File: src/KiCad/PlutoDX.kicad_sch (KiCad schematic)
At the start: 0 parts

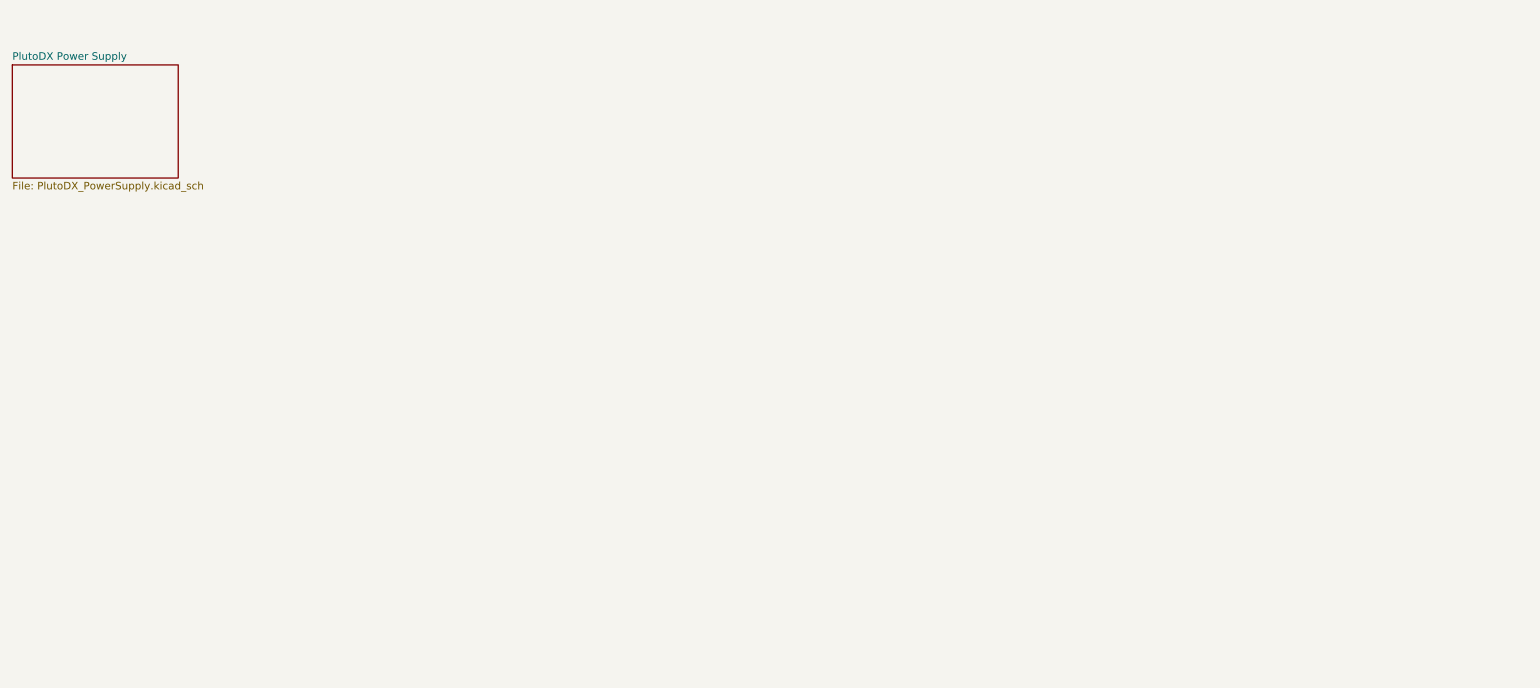
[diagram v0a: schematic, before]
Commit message: Import SOM304RD-VI symbol from the weeCee project
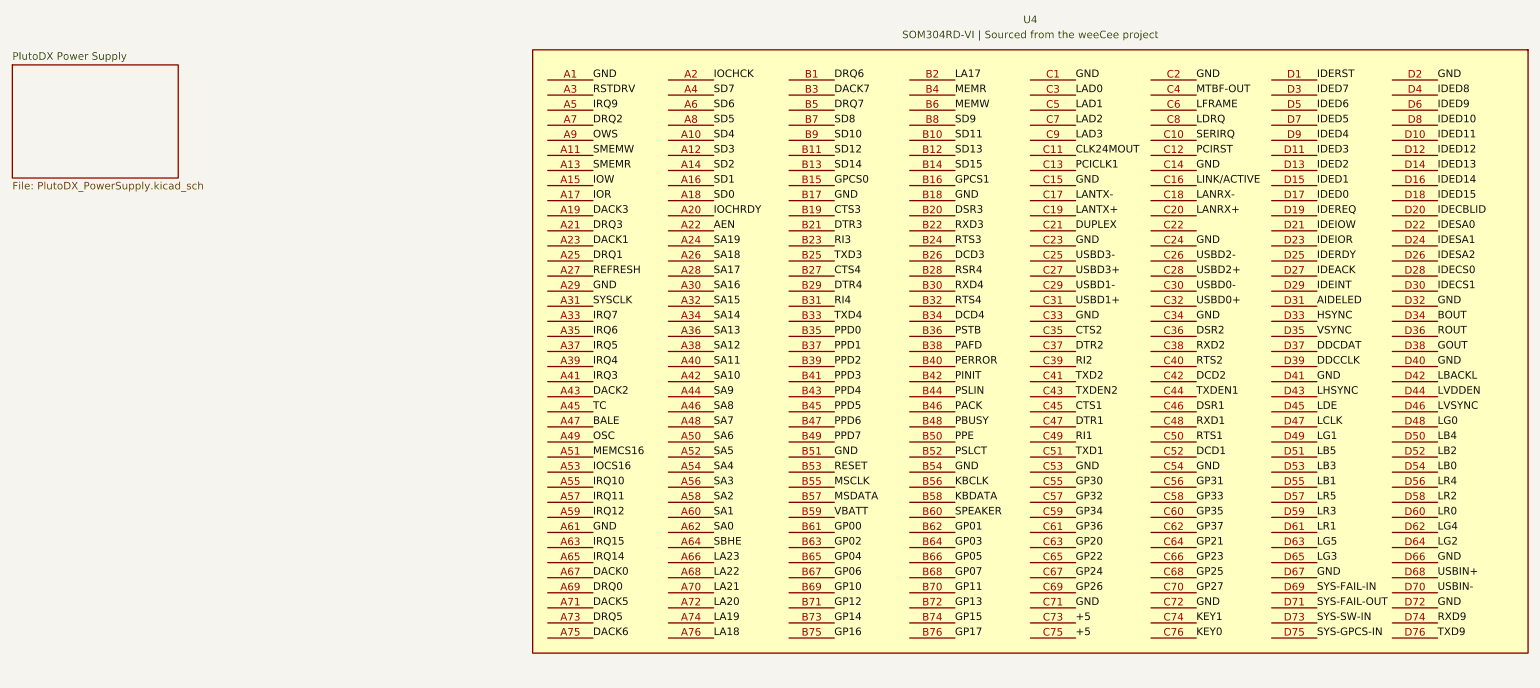
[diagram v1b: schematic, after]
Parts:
- added U4: SOM304RD-VI | Sourced from the weeCee project, Quad20, symbol SOM304RD-VI:SYM-7hfih1o77usjfiwb5d4g-1
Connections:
- new net +5: U4.C73, U4.C75
- new net AEN: U4.A22
- new net AIDELED: U4.D31
- new net BALE: U4.A47
- new net BOUT: U4.D34
- new net CLK24MOUT: U4.C11
- new net CTS1: U4.C45
- new net CTS2: U4.C35
- new net CTS3: U4.B19
- new net CTS4: U4.B27
- new net DACK0: U4.A67
- new net DACK1: U4.A23
- new net DACK2: U4.A43
- new net DACK3: U4.A19
- new net DACK5: U4.A71
- new net DACK6: U4.A75
- new net DACK7: U4.B3
- new net DCD1: U4.C52
- new net DCD2: U4.C42
- new net DCD3: U4.B26
- new net DCD4: U4.B34
- new net DDCCLK: U4.D39
- new net DDCDAT: U4.D37
- new net DRQ0: U4.A69
- new net DRQ1: U4.A25
- new net DRQ2: U4.A7
- new net DRQ3: U4.A21
- new net DRQ5: U4.A73
- new net DRQ6: U4.B1
- new net DRQ7: U4.B5
- new net DSR1: U4.C46
- new net DSR2: U4.C36
- new net DSR3: U4.B20
- new net DTR1: U4.C47
- new net DTR2: U4.C37
- new net DTR3: U4.B21
- new net DTR4: U4.B29
- new net DUPLEX: U4.C21
- new net GND: U4.A1, U4.A29, U4.A61, U4.B17, U4.B18, U4.B51, U4.B54, U4.C1, U4.C14, U4.C15, U4.C2, U4.C23, U4.C24, U4.C33, U4.C34, U4.C53, U4.C54, U4.C71, U4.C72, U4.D2, U4.D32, U4.D40, U4.D41, U4.D66, U4.D67, U4.D72
- new net GOUT: U4.D38
- new net GP00: U4.B61
- new net GP01: U4.B62
- new net GP02: U4.B63
- new net GP03: U4.B64
- new net GP04: U4.B65
- new net GP05: U4.B66
- new net GP06: U4.B67
- new net GP07: U4.B68
- new net GP10: U4.B69
- new net GP11: U4.B70
- new net GP12: U4.B71
- new net GP13: U4.B72
- new net GP14: U4.B73
- new net GP15: U4.B74
- new net GP16: U4.B75
- new net GP17: U4.B76
- new net GP20: U4.C63
- new net GP21: U4.C64
- new net GP22: U4.C65
- new net GP23: U4.C66
- new net GP24: U4.C67
- new net GP25: U4.C68
- new net GP26: U4.C69
- new net GP27: U4.C70
- new net GP30: U4.C55
- new net GP31: U4.C56
- new net GP32: U4.C57
- new net GP33: U4.C58
- new net GP34: U4.C59
- new net GP35: U4.C60
- new net GP36: U4.C61
- new net GP37: U4.C62
- new net GPCS0: U4.B15
- new net GPCS1: U4.B16
- new net HSYNC: U4.D33
- new net IDEACK: U4.D27
- new net IDECBLID: U4.D20
- new net IDECS0: U4.D28
- new net IDECS1: U4.D30
- new net IDED0: U4.D17
- new net IDED1: U4.D15
- new net IDED10: U4.D8
- new net IDED11: U4.D10
- new net IDED12: U4.D12
- new net IDED13: U4.D14
- new net IDED14: U4.D16
- new net IDED15: U4.D18
- new net IDED2: U4.D13
- new net IDED3: U4.D11
- new net IDED4: U4.D9
- new net IDED5: U4.D7
- new net IDED6: U4.D5
- new net IDED7: U4.D3
- new net IDED8: U4.D4
- new net IDED9: U4.D6
- new net IDEINT: U4.D29
- new net IDEIOR: U4.D23
- new net IDEIOW: U4.D21
- new net IDERDY: U4.D25
- new net IDEREQ: U4.D19
- new net IDERST: U4.D1
- new net IDESA0: U4.D22
- new net IDESA1: U4.D24
- new net IDESA2: U4.D26
- new net IOCHCK: U4.A2
- new net IOCHRDY: U4.A20
- new net IOCS16: U4.A53
- new net IOR: U4.A17
- new net IOW: U4.A15
- new net IRQ10: U4.A55
- new net IRQ11: U4.A57
- new net IRQ12: U4.A59
- new net IRQ14: U4.A65
- new net IRQ15: U4.A63
- new net IRQ3: U4.A41
- new net IRQ4: U4.A39
- new net IRQ5: U4.A37
- new net IRQ6: U4.A35
- new net IRQ7: U4.A33
- new net IRQ9: U4.A5
- new net KBCLK: U4.B56
- new net KBDATA: U4.B58
- new net KEY0: U4.C76
- new net KEY1: U4.C74
- new net LA17: U4.B2
- new net LA18: U4.A76
- new net LA19: U4.A74
- new net LA20: U4.A72
- new net LA21: U4.A70
- new net LA22: U4.A68
- new net LA23: U4.A66
- new net LAD0: U4.C3
- new net LAD1: U4.C5
- new net LAD2: U4.C7
- new net LAD3: U4.C9
- new net LANRX+: U4.C20
- new net LANRX-: U4.C18
- new net LANTX+: U4.C19
- new net LANTX-: U4.C17
- new net LB0: U4.D54
- new net LB1: U4.D55
- new net LB2: U4.D52
- new net LB3: U4.D53
- new net LB4: U4.D50
- new net LB5: U4.D51
- new net LBACKL: U4.D42
- new net LCLK: U4.D47
- new net LDE: U4.D45
- new net LDRQ: U4.C8
- new net LFRAME: U4.C6
- new net LG0: U4.D48
- new net LG1: U4.D49
- new net LG2: U4.D64
- new net LG3: U4.D65
- new net LG4: U4.D62
- new net LG5: U4.D63
- new net LHSYNC: U4.D43
- new net LINK/ACTIVE: U4.C16
- new net LR0: U4.D60
- new net LR1: U4.D61
- new net LR2: U4.D58
- new net LR3: U4.D59
- new net LR4: U4.D56
- new net LR5: U4.D57
- new net LVDDEN: U4.D44
- new net LVSYNC: U4.D46
- new net MEMCS16: U4.A51
- new net MEMR: U4.B4
- new net MEMW: U4.B6
- new net MSCLK: U4.B55
- new net MSDATA: U4.B57
- new net MTBF-OUT: U4.C4
- new net OSC: U4.A49
- new net OWS: U4.A9
- new net PACK: U4.B46
- new net PAFD: U4.B38
- new net PBUSY: U4.B48
- new net PCICLK1: U4.C13
- new net PCIRST: U4.C12
- new net PERROR: U4.B40
- new net PINIT: U4.B42
- new net PPD0: U4.B35
- new net PPD1: U4.B37
- new net PPD2: U4.B39
- new net PPD3: U4.B41
- new net PPD4: U4.B43
- new net PPD5: U4.B45
- new net PPD6: U4.B47
- new net PPD7: U4.B49
- new net PPE: U4.B50
- new net PSLCT: U4.B52
- new net PSLIN: U4.B44
- new net PSTB: U4.B36
- new net REFRESH: U4.A27
- new net RESET: U4.B53
- new net RI1: U4.C49
- new net RI2: U4.C39
- new net RI3: U4.B23
- new net RI4: U4.B31
- new net ROUT: U4.D36
- new net RSR4: U4.B28
- new net RSTDRV: U4.A3
- new net RTS1: U4.C50
- new net RTS2: U4.C40
- new net RTS3: U4.B24
- new net RTS4: U4.B32
- new net RXD1: U4.C48
- new net RXD2: U4.C38
- new net RXD3: U4.B22
- new net RXD4: U4.B30
- new net RXD9: U4.D74
- new net SA0: U4.A62
- new net SA1: U4.A60
- new net SA10: U4.A42
- new net SA11: U4.A40
- new net SA12: U4.A38
- new net SA13: U4.A36
- new net SA14: U4.A34
- new net SA15: U4.A32
- new net SA16: U4.A30
- new net SA17: U4.A28
- new net SA18: U4.A26
- new net SA19: U4.A24
- new net SA2: U4.A58
- new net SA3: U4.A56
- new net SA4: U4.A54
- new net SA5: U4.A52
- new net SA6: U4.A50
- new net SA7: U4.A48
- new net SA8: U4.A46
- new net SA9: U4.A44
- new net SBHE: U4.A64
- new net SD0: U4.A18
- new net SD1: U4.A16
- new net SD10: U4.B9
- new net SD11: U4.B10
- new net SD12: U4.B11
- new net SD13: U4.B12
- new net SD14: U4.B13
- new net SD15: U4.B14
- new net SD2: U4.A14
- new net SD3: U4.A12
- new net SD4: U4.A10
- new net SD5: U4.A8
- new net SD6: U4.A6
- new net SD7: U4.A4
- new net SD8: U4.B7
- new net SD9: U4.B8
- new net SERIRQ: U4.C10
- new net SMEMR: U4.A13
- new net SMEMW: U4.A11
- new net SPEAKER: U4.B60
- new net SYS-FAIL-IN: U4.D69
- new net SYS-FAIL-OUT: U4.D71
- new net SYS-GPCS-IN: U4.D75
- new net SYS-SW-IN: U4.D73
- new net SYSCLK: U4.A31
- new net TC: U4.A45
- new net TXD1: U4.C51
- new net TXD2: U4.C41
- new net TXD3: U4.B25
- new net TXD4: U4.B33
- new net TXD9: U4.D76
- new net TXDEN1: U4.C44
- new net TXDEN2: U4.C43
- new net USBD0+: U4.C32
- new net USBD0-: U4.C30
- new net USBD1+: U4.C31
- new net USBD1-: U4.C29
- new net USBD2+: U4.C28
- new net USBD2-: U4.C26
- new net USBD3+: U4.C27
- new net USBD3-: U4.C25
- new net USBIN+: U4.D68
- new net USBIN-: U4.D70
- new net VBATT: U4.B59
- new net VSYNC: U4.D35

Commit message: Start SD-IDE interface
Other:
- added sheet PlutoDX SD to IDE Interface (PlutoDX_SD2IDE-Interface.kicad_sch)
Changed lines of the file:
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@@
+		)
+	)
+	(sheet
+		(at 24.13 54.61)
+		(size 27.94 19.05)
+		(exclude_from_sim no)
+		(in_bom yes)
+		(on_board yes)
+		(dnp no)
+		(fields_autoplaced yes)
+		(stroke
+			(width 0.1524)
+			(type solid)
+		)
+		(fill
+			(color 0 0 0 0)
+		)
+		(property "Sheetname" "PlutoDX SD to IDE Interface"
+			(at 24.13 53.8984 0)
+			(show_name no)
+			(do_not_autoplace no)
+			(effects
+				(font
+					(size 1.27 1.27)
+				)
+				(justify left bottom)
+			)
+		)
+		(property "Sheetfile" "PlutoDX_SD2IDE-Interface.kicad_sch"
+			(at 24.13 74.2446 0)
+			(show_name no)
+			(do_not_autoplace no)
+			(effects
+				(font
+					(size 1.27 1.27)
+				)
+				(justify left top)
+			)
+		)
+		(property "Field2" ""
+			(at 24.13 54.61 0)
+			(hide yes)
+			(show_name no)
+			(do_not_autoplace no)
+			(effects
+				(font
+					(size 1.27 1.27)
+				)
+			)
+		)
+		(property "Field3" ""
+			(at 24.13 54.61 0)
+			(hide yes)
+			(show_name no)
+			(do_not_autoplace no)
+			(effects
+				(font
+					(size 1.27 1.27)
+				)
+			)
+		)
+		(instances
+			(project "PlutoDX"
+				(path "/68463962-111b-48d5-8810-5302d4be8c60"
+					(page "3")
+				)
+			)
 		)
 	)

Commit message: Start serial & parallel
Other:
- added sheet PlutoDX Serial & Parallel IO (PlutoDX_IO-Serial-Parallel.kicad_sch)
- added sheet PlutoDX Video (PlutoDX_Video.kicad_sch)
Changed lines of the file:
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@@
+	)
+	(sheet
+		(at 24.13 81.28)
+		(size 27.94 19.05)
+		(exclude_from_sim no)
+		(in_bom yes)
+		(on_board yes)
+		(dnp no)
+		(fields_autoplaced yes)
+		(stroke
+			(width 0.1524)
+			(type solid)
+		)
+		(fill
+			(color 0 0 0 0)
+		)
+		(property "Sheetname" "PlutoDX Video"
+			(at 24.13 80.5684 0)
+			(show_name no)
+			(do_not_autoplace no)
+			(effects
+				(font
+					(size 1.27 1.27)
+				)
+				(justify left bottom)
+			)
+		)
+		(property "Sheetfile" "PlutoDX_Video.kicad_sch"
+			(at 24.13 100.9146 0)
+			(show_name no)
+			(do_not_autoplace no)
+			(effects
+				(font
+					(size 1.27 1.27)
+				)
+				(justify left top)
+			)
+		)
+		(instances
+			(project "PlutoDX"
+				(path "/68463962-111b-48d5-8810-5302d4be8c60"
+					(page "4")
+				)
+			)
+		)
 	)
 	(sheet
@@
 				)
 			)
+		)
+	)
+	(sheet
+		(at 24.13 106.68)
+		(size 27.94 20.32)
+		(exclude_from_sim no)
+		(in_bom yes)
+		(on_board yes)
+		(dnp no)
+		(fields_autoplaced yes)
+		(stroke
+			(width 0.1524)
+			(type solid)
+		)
+		(fill
+			(color 0 0 0 0)
+		)
+		(property "Sheetname" "PlutoDX Serial & Parallel IO"
+			(at 24.13 105.9684 0)
+			(show_name no)
+			(do_not_autoplace no)
+			(effects
+				(font
+					(size 1.27 1.27)
+				)
+				(justify left bottom)
+			)
+		)
+		(property "Sheetfile" "PlutoDX_IO-Serial-Parallel.kicad_sch"
+			(at 24.13 127.5846 0)
+			(show_name no)
+			(do_not_autoplace no)
+			(effects
+				(font
+					(size 1.27 1.27)
+				)
+				(justify left top)
+			)
+		)
+		(instances
+			(project "PlutoDX"
+				(path "/68463962-111b-48d5-8810-5302d4be8c60"
+					(page "5")
+				)
+			)

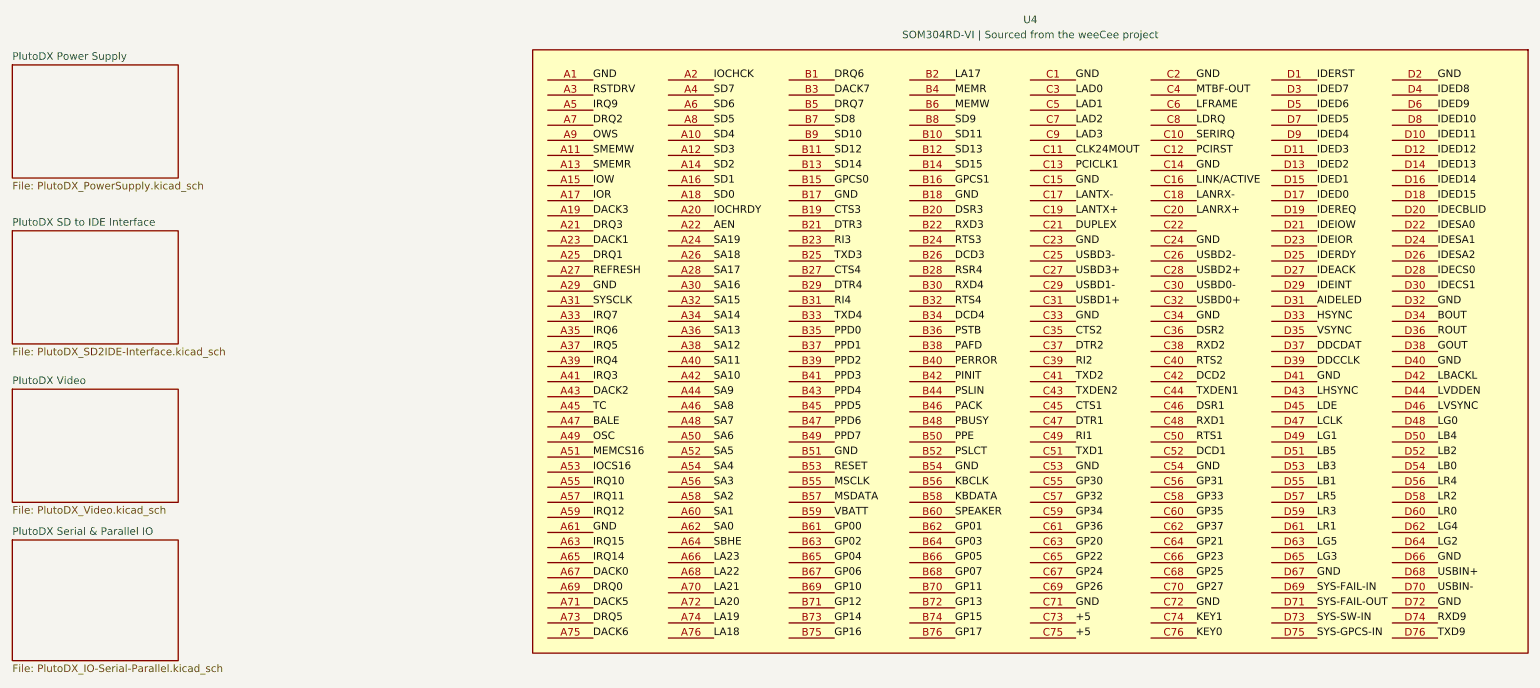
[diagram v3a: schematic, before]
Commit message: Switch to SOM304RD-PI fro mSOM304RD-VI
The SOM304RD-PI exposes a PCI bus, so PCI cards can be added. Video will now be handled via a PCI video card and/or 3D accelerator vs the SOM304RD-VI's built-in VGA video output
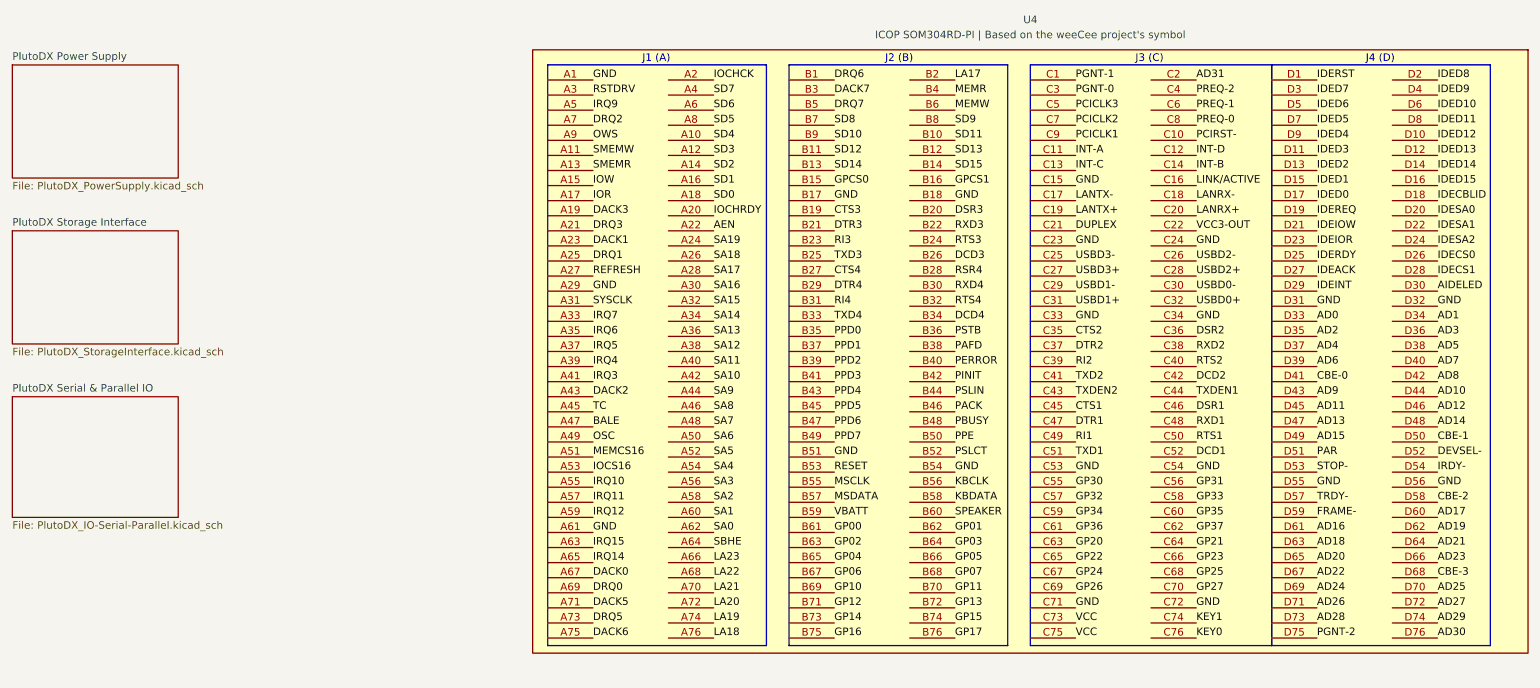
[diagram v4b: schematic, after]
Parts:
- U4: value SOM304RD-VI | Sourced from the weeCee project -> ICOP SOM304RD-PI | Based on the weeCee project's symbol
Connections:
- net LAD3 is gone; now on net PCICLK1: U4.C9
- net LB1 is gone; now on net GND: U4.D55
- net LR4 is gone; now on net GND: U4.D56
- net AIDELED: now also U4.D30; no longer U4.D31
- net GND: now also U4.D31; no longer U4.C1, U4.C14, U4.C2, U4.D2, U4.D40, U4.D41, U4.D66, U4.D67, U4.D72
- net IDECBLID: now also U4.D18; no longer U4.D20
- net IDECS0: now also U4.D26; no longer U4.D28
- net IDECS1: now also U4.D28; no longer U4.D30
- net IDED10: now also U4.D6; no longer U4.D8
- net IDED11: now also U4.D8; no longer U4.D10
- net IDED12: now also U4.D10; no longer U4.D12
- net IDED13: now also U4.D12; no longer U4.D14
- net IDED14: now also U4.D14; no longer U4.D16
- net IDED15: now also U4.D16; no longer U4.D18
- net IDED8: now also U4.D2; no longer U4.D4
- net IDED9: now also U4.D4; no longer U4.D6
- net IDESA0: now also U4.D20; no longer U4.D22
- net IDESA1: now also U4.D22; no longer U4.D24
- net IDESA2: now also U4.D24; no longer U4.D26
- net PCICLK1: no longer U4.C13
- net VCC3-OUT: now reaches U4.C22
- net +5 renamed VCC
- net BOUT renamed AD1
- net CLK24MOUT renamed INT-A
- net DDCCLK renamed AD6
- net DDCDAT renamed AD4
- net GOUT renamed AD5
- net HSYNC renamed AD0
- net LAD0 renamed PGNT-0
- net LAD1 renamed PCICLK3
- net LAD2 renamed PCICLK2
- net LB0 renamed IRDY-
- net LB2 renamed DEVSEL-
- net LB3 renamed STOP-
- net LB4 renamed CBE-1
- net LB5 renamed PAR
- net LBACKL renamed AD8
- net LCLK renamed AD13
- net LDE renamed AD11
- net LDRQ renamed PREQ-0
- net LFRAME renamed PREQ-1
- net LG0 renamed AD14
- net LG1 renamed AD15
- net LG2 renamed AD21
- net LG3 renamed AD20
- net LG4 renamed AD19
- net LG5 renamed AD18
- net LHSYNC renamed AD9
- net LR0 renamed AD17
- net LR1 renamed AD16
- net LR2 renamed CBE-2
- net LR3 renamed FRAME-
- net LR5 renamed TRDY-
- net LVDDEN renamed AD10
- net LVSYNC renamed AD12
- net MTBF-OUT renamed PREQ-2
- net PCIRST renamed INT-D
- net ROUT renamed AD3
- net RXD9 renamed AD29
- net SERIRQ renamed PCIRST-
- net SYS-FAIL-IN renamed AD24
- net SYS-FAIL-OUT renamed AD26
- net SYS-GPCS-IN renamed PGNT-2
- net SYS-SW-IN renamed AD28
- net TXD9 renamed AD30
- net USBIN+ renamed CBE-3
- net USBIN- renamed AD25
- net VSYNC renamed AD2
- new net AD22: U4.D67
- new net AD23: U4.D66
- new net AD27: U4.D72
- new net AD31: U4.C2
- new net AD7: U4.D40
- new net CBE-0: U4.D41
- new net INT-B: U4.C14
- new net INT-C: U4.C13
- new net PGNT-1: U4.C1
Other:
- sheet PlutoDX SD to IDE Interface renamed PlutoDX Storage Interface
- removed sheet PlutoDX Video
- sheet PlutoDX Storage Interface: file PlutoDX_SD2IDE-Interface.kicad_sch -> PlutoDX_StorageInterface.kicad_sch
- note added: "J1 (A)"
- note added: "J2 (B)"
- note added: "J3 (C)"
- note added: "J4 (D)"
